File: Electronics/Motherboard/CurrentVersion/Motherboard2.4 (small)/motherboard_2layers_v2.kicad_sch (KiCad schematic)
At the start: 87 parts, among them J1 Conn_02x10_Odd_Even, J2 SSD1306, J3 USB_C_Receptacle_USB2.0_16P, J4 Micro_SD_Card_Det2, J5 Encoder, Q1 FDMS86202, Q2 FDMS86202, Q3 AO3400A, Q4 AO3400A, Q5 AO3400A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

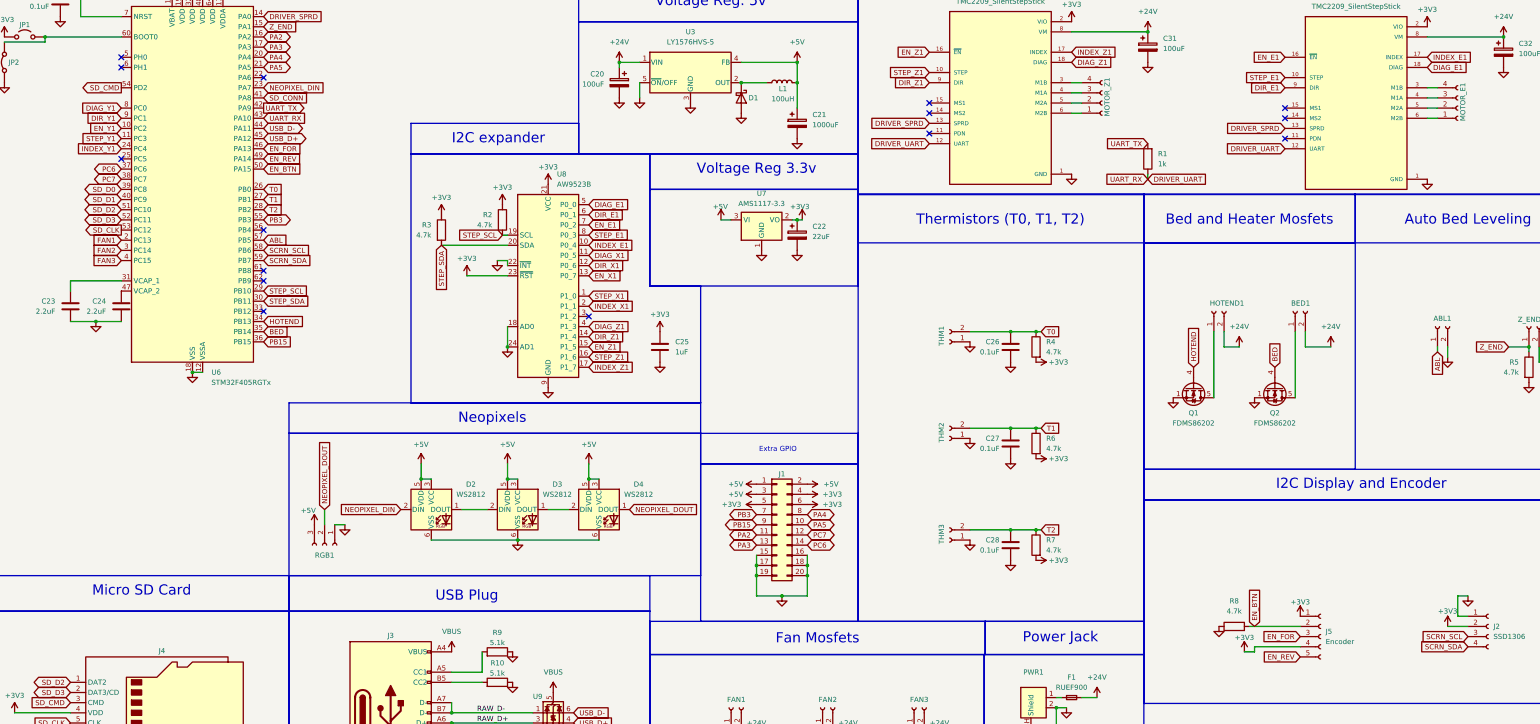
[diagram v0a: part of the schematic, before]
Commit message: Changed motherboard to accomidate klipper
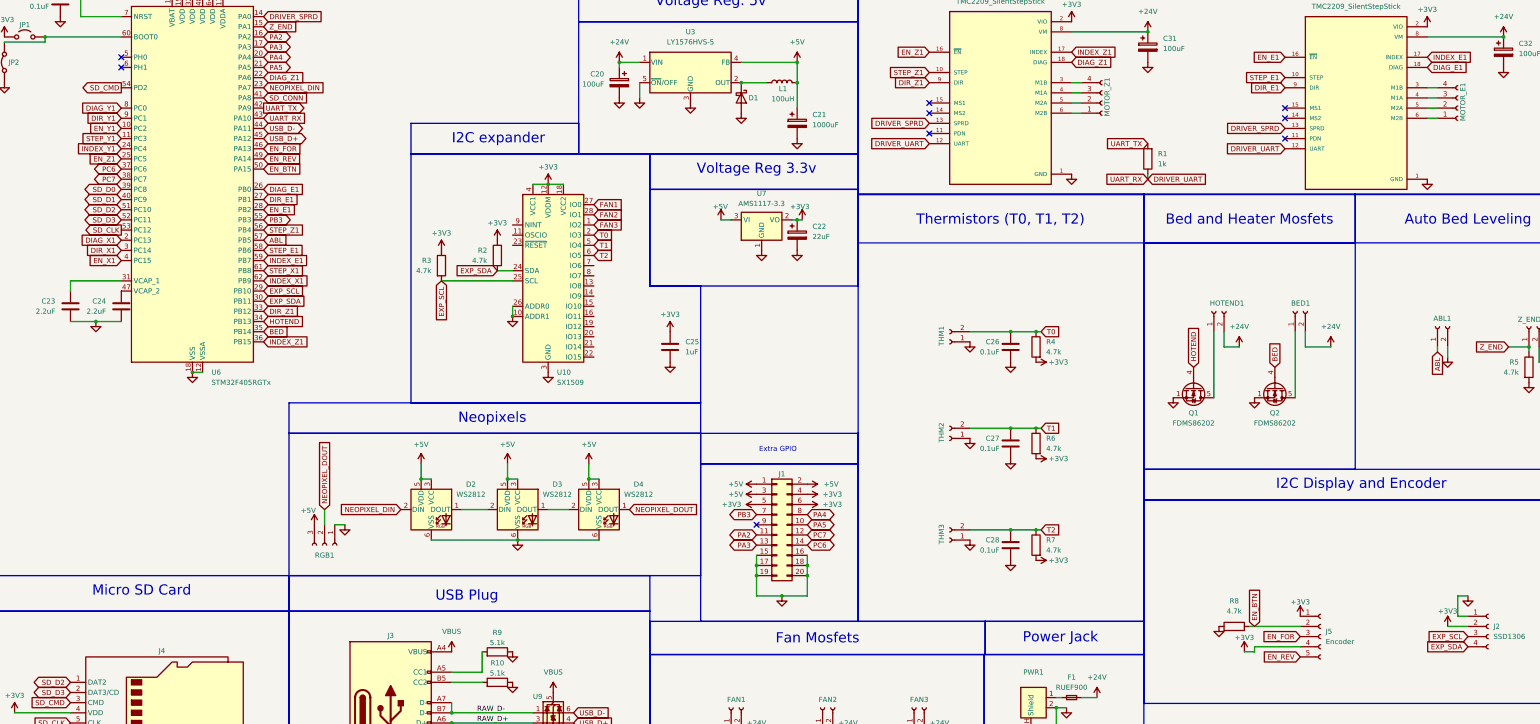
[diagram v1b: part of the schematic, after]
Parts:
- removed U8: AW9523B, Package_DFN_QFN:QFN-24-1EP_4x4mm_P0.5mm_EP2.7x2.7mm, symbol Interface_Expansion:AW9523B
- added U10: SX1509, Package_DFN_QFN:QFN-28-1EP_4x4mm_P0.4mm_EP2.6x2.6mm, symbol ad-hoc:SX1509
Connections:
- net +3V3: now also U10.12 (VDDM), U10.18 (VCC2), U10.4 (VCC1)
- net DIAG_E1: now also U6.26 (PB0)
- net DIAG_X1: now also U6.2 (PC13)
- net DIAG_Z1: now also U6.22 (PA6)
- net DIR_E1: now also U6.27 (PB1)
- net DIR_X1: now also U6.3 (PC14)
- net DIR_Z1: now also U6.33 (PB12)
- net EN_E1: now also U6.28 (PB2)
- net EN_X1: now also U6.4 (PC15)
- net EN_Z1: now also U6.25 (PC5)
- net FAN1: now also U10.27 (IO0); no longer U6.2 (PC13)
- net FAN2: now also U10.28 (IO1); no longer U6.3 (PC14)
- net FAN3: now also U10.1 (IO2); no longer U6.4 (PC15)
- net GND: now also U10.10 (ADDR1), U10.17 (GND), U10.26 (ADDR0), U10.3 (GND)
- net INDEX_E1: now also U6.59 (PB7)
- net INDEX_X1: now also U6.62 (PB9)
- net INDEX_Z1: now also U6.36 (PB15)
- net STEP_E1: now also U6.58 (PB6)
- net STEP_X1: now also U6.61 (PB8)
- net STEP_Z1: now also U6.56 (PB4)
- net T0: now also U10.2 (IO3); no longer U6.26 (PB0)
- net T1: now also U10.5 (IO4); no longer U6.27 (PB1)
- net T2: now also U10.6 (IO5); no longer U6.28 (PB2)
- net PB15: no longer names the net of J1.9 (Pin_9)
- net PB15: no longer U6.36 (PB15)
- net SCRN_SCL renamed EXP_SCL
- net EXP_SCL: now also R3.2, U6.29 (PB10), U10.25 (SCL); no longer U6.58 (PB6)
- net SCRN_SDA renamed EXP_SDA
- net EXP_SDA: now also R2.2, U6.30 (PB11), U10.24 (SDA); no longer U6.59 (PB7)
- removed net STEP_SCL: R2.2, U6.29 (PB10)
- removed net STEP_SDA: R3.2, U6.30 (PB11)
- no-connect marks 23 -> 17
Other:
- moved on the sheet: C25, R2, R3

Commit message: klipper and slight changes to schematic
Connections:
- net +3V3: now also U2.14 (MS2), U4.15 (MS1), U5.14 (MS2), U5.15 (MS1)
- no-connect marks 17 -> 23

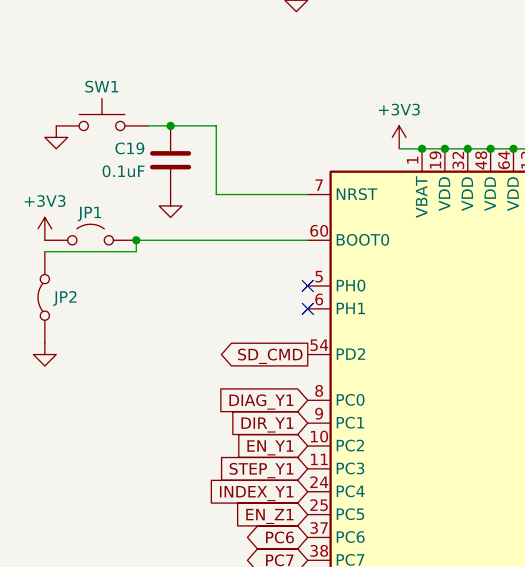
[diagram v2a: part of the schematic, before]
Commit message: changes so we can more easily access the bootloader when flashing
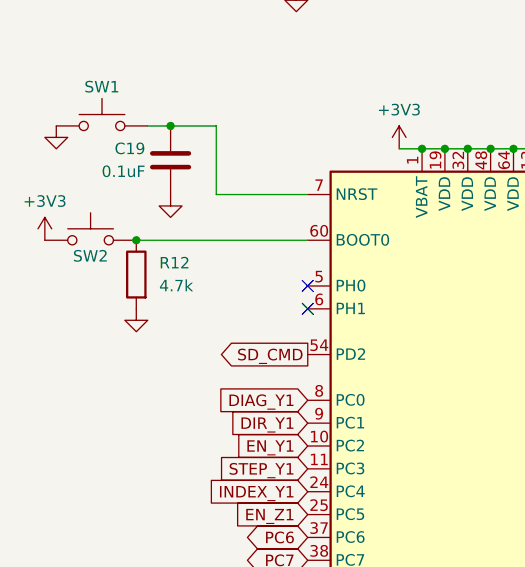
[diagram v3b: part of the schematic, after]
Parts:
- removed JP1: Jumper_2_Open, TestPoint:TestPoint_2Pads_Pitch2.54mm_Drill0.8mm, symbol Jumper:Jumper_2_Open
- removed JP2: Jumper_2_Bridged, TestPoint:TestPoint_2Pads_Pitch2.54mm_Drill0.8mm, symbol Jumper:Jumper_2_Bridged
- added R12: 4.7k, Resistor_SMD:R_0603_1608Metric, symbol Device:R
- added SW2: ~, ad-hoc:ALPSALPINE_TopPush_Button, symbol Switch:SW_Push
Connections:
- net +3V3: now also SW2.1
- net GND: now also R12.2
- net at U6.60 (BOOT0): now also R12.1, SW2.2
